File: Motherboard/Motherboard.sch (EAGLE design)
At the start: 12 parts

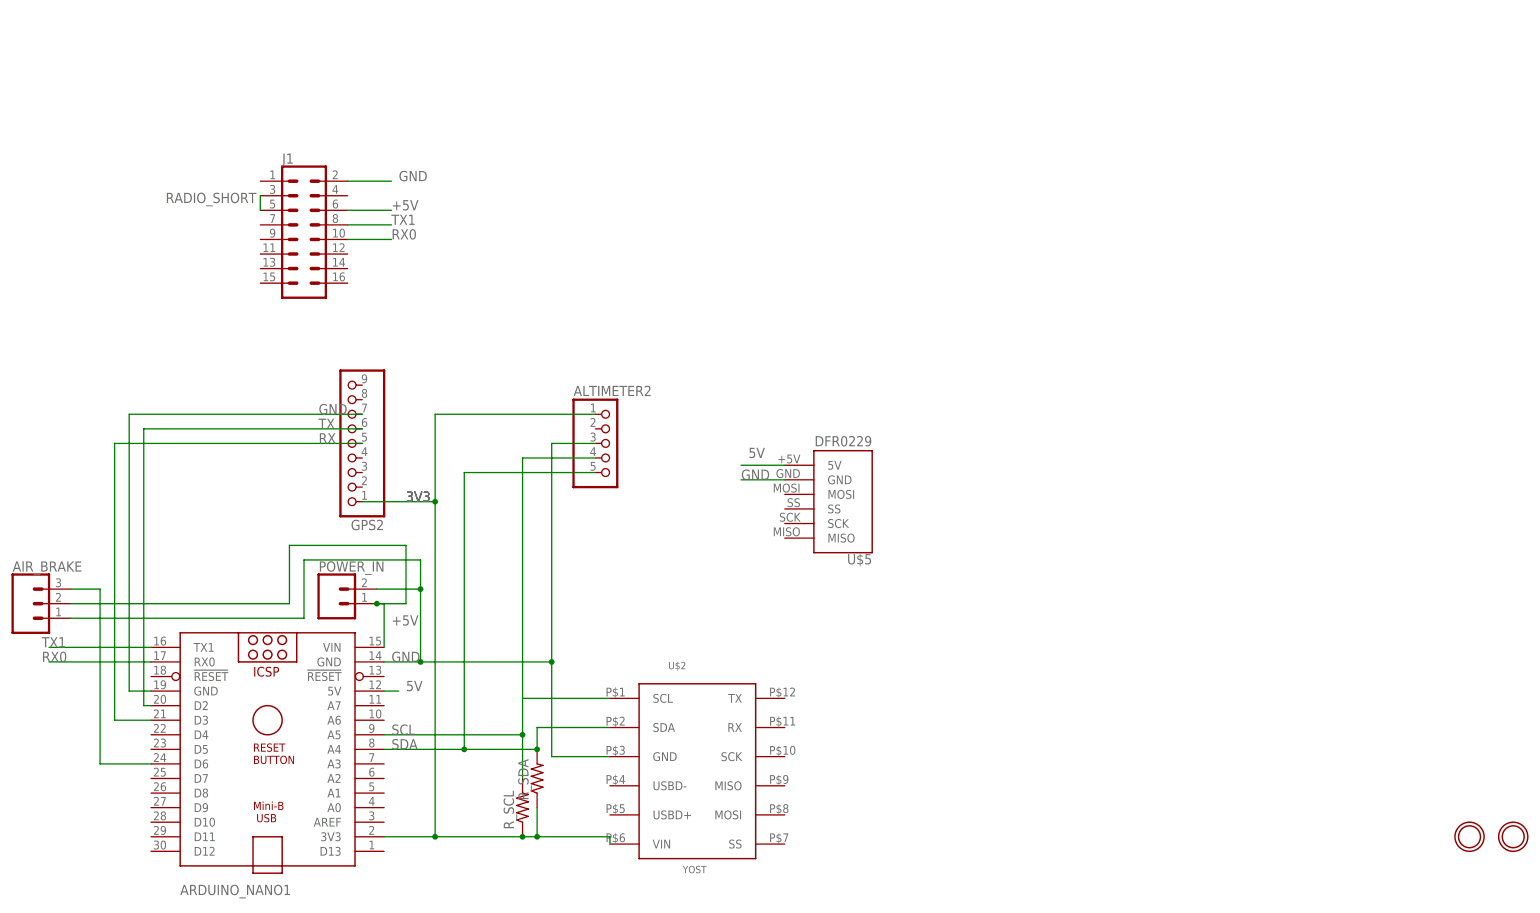
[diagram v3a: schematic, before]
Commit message: add components to boards
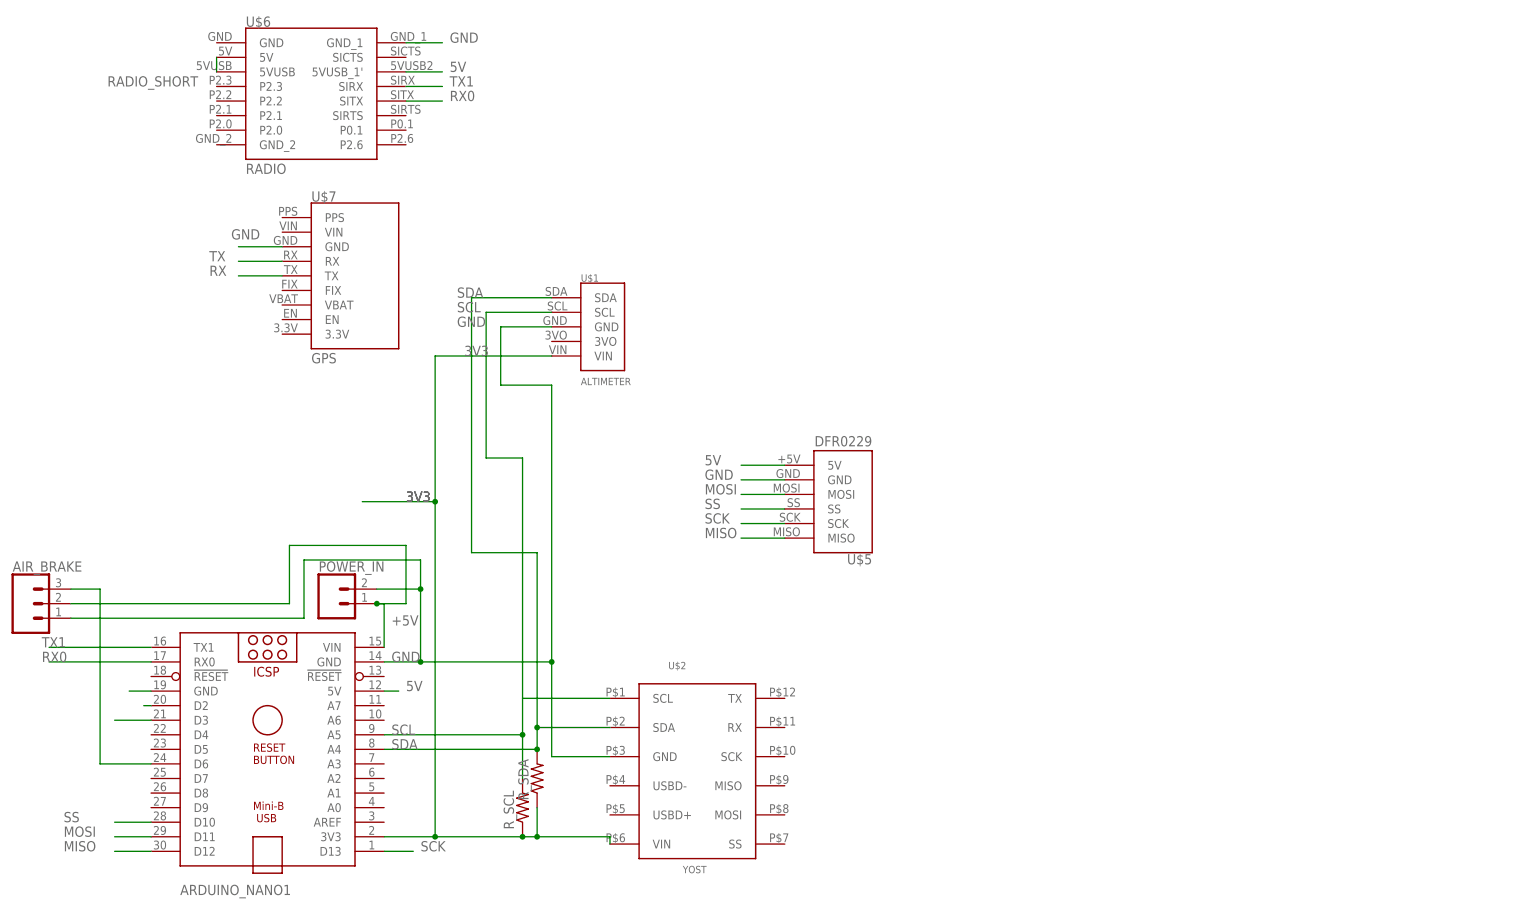
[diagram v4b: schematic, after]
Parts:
- removed ALTIMETER2: (no value), microbuilder:HEADER-1X570MIL
- removed GPS2: (no value), microbuilder:HEADER-1X970MIL
- removed J1: (no value), SparkFun-Connectors:CONN_08X2_HEADER
- removed U$3, U$4: MOUNTINGHOLE2.5, microbuilder:MOUNTINGHOLE2.5
- added U$1: ALTIMETER, uORocketry-parts:ALTIMETER
- added U$6: RADIO, uORocketry-parts:RADIO
- added U$7: GPS, uORocketry-parts:GPS
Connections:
- new net MISO: ARDUINO_NANO1.D12, U$5.MISO
- new net MOSI: ARDUINO_NANO1.D11, U$5.MOSI
- new net SCK: ARDUINO_NANO1.D13, U$5.SCK
- new net SS: ARDUINO_NANO1.D10, U$5.SS
- net +5V: no longer J1.6
- net 3V3: now also U$1.VIN; no longer ALTIMETER2.1, GPS2.1
- net 5V: now also U$6.5VUSB_1'
- net GND: now also U$1.GND, U$6.GND_1, U$7.GND; no longer ALTIMETER2.3, GPS2.7, J1.2
- net RADIO_SHORT: now also U$6.5V, U$6.5VUSB; no longer J1.3, J1.5
- net RX: now also U$7.TX; no longer GPS2.5
- net RX0: now also U$6.SITX; no longer J1.10
- net SCL: now also U$1.SCL; no longer ALTIMETER2.4
- net SDA: now also U$1.SDA; no longer ALTIMETER2.5
- net TX: now also U$7.RX; no longer GPS2.6
- net TX1: now also U$6.SIRX; no longer J1.8

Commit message: more layout
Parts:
- added U$3: RS232, uORocketry-parts:RS232
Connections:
- new net SBG_RX: ARDUINO_NANO1.D5, U$3.RX-1
- new net SBG_TX: ARDUINO_NANO1.D4, U$3.TX-0
- net 5V: now also U$3.VCC
- net GND: now also U$3.GND
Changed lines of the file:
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@@
 <setting verticaltext="up"/>
 </settings>
-<grid distance="0.05" unitdist="inch" unit="inch" style="lines" multiple="1" display="no" altdistance="0.01" altunitdist="inch" altunit="inch"/>
+<grid distance="0.1" unitdist="inch" unit="inch" style="lines" multiple="1" display="no" altdistance="0.01" altunitdist="inch" altunit="inch"/>
 <layers>
 <layer number="1" name="Top" color="4" fill="1" visible="no" active="no"/>
@@
 <part name="U$1" library="uORocketry-parts" deviceset="ALTIMETER" device=""/>
 <part name="U$7" library="uORocketry-parts" deviceset="GPS" device=""/>
+<part name="U$3" library="uORocketry-parts" deviceset="RS232" device=""/>
 </parts>
 <sheets>
@@
 <attribute name="VALUE" x="-34.29" y="57.15" size="1.778" layer="96"/>
 </instance>
+<instance part="U$3" gate="G$1" x="33.02" y="93.98" smashed="yes"/>
 </instances>
 <busses>
@@
 <label x="-48.26" y="78.74" size="1.778" layer="95"/>
 </segment>
+<segment>
+<pinref part="U$3" gate="G$1" pin="GND"/>
+<wire x1="22.86" y1="96.52" x2="15.24" y2="96.52" width="0.1524" layer="91"/>
+<label x="12.7" y="96.52" size="1.778" layer="95"/>
+</segment>
 </net>
 <net name="SDA" class="0">
@@
 <label x="-10.16" y="107.95" size="1.778" layer="95"/>
 </segment>
+<segment>
+<pinref part="U$3" gate="G$1" pin="VCC"/>
+<wire x1="22.86" y1="101.6" x2="15.24" y2="101.6" width="0.1524" layer="91"/>
+<label x="12.7" y="101.6" size="1.778" layer="95"/>
+</segment>
 </net>
 <net name="SCK" class="0">
@@
 </segment>
 </net>
+<net name="SBG_TX" class="0">
+<segment>
+<pinref part="ARDUINO_NANO1" gate="G$1" pin="D4"/>
+<wire x1="-62.23" y1="-7.62" x2="-68.58" y2="-7.62" width="0.1524" layer="91"/>
+<label x="-81.28" y="-7.62" size="1.778" layer="95"/>
+</segment>
+<segment>
+<pinref part="U$3" gate="G$1" pin="TX-0"/>
+<wire x1="22.86" y1="91.44" x2="15.24" y2="91.44" width="0.1524" layer="91"/>
+<label x="5.08" y="91.44" size="1.778" layer="95"/>
+</segment>
+</net>
+<net name="SBG_RX" class="0">
+<segment>
+<pinref part="ARDUINO_NANO1" gate="G$1" pin="D5"/>
+<wire x1="-62.23" y1="-10.16" x2="-68.58" y2="-10.16" width="0.1524" layer="91"/>
+<label x="-81.28" y="-10.16" size="1.778" layer="95"/>
+</segment>
+<segment>
+<pinref part="U$3" gate="G$1" pin="RX-1"/>
+<wire x1="22.86" y1="86.36" x2="15.24" y2="86.36" width="0.1524" layer="91"/>
+<label x="5.08" y="86.36" size="1.778" layer="95"/>
+</segment>
+</net>

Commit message: review1
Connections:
- net SBG_RX: now also ARDUINO_NANO1.D9; no longer ARDUINO_NANO1.D5
- net SBG_TX: now also ARDUINO_NANO1.D8; no longer ARDUINO_NANO1.D4
- net SS: now also ARDUINO_NANO1.D4; no longer ARDUINO_NANO1.D10
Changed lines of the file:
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@@
 <net name="SS" class="0">
-<segment>
-<pinref part="ARDUINO_NANO1" gate="G$1" pin="D10"/>
-<wire x1="-62.23" y1="-22.86" x2="-68.58" y2="-22.86" width="0.1524" layer="91"/>
-<label x="-77.47" y="-22.86" size="1.778" layer="95"/>
-</segment>
 <segment>
 <pinref part="U$5" gate="G$1" pin="SS"/>
@@
 <label x="34.29" y="31.75" size="1.778" layer="95"/>
 </segment>
-</net>
-<net name="SBG_TX" class="0">
 <segment>
 <pinref part="ARDUINO_NANO1" gate="G$1" pin="D4"/>
 <wire x1="-62.23" y1="-7.62" x2="-68.58" y2="-7.62" width="0.1524" layer="91"/>
-<label x="-81.28" y="-7.62" size="1.778" layer="95"/>
+<label x="-76.2" y="-7.62" size="1.778" layer="95"/>
 </segment>
+</net>
+<net name="SBG_TX" class="0">
 <segment>
 <pinref part="U$3" gate="G$1" pin="TX-0"/>
@@
 <label x="5.08" y="91.44" size="1.778" layer="95"/>
 </segment>
+<segment>
+<pinref part="ARDUINO_NANO1" gate="G$1" pin="D8"/>
+<wire x1="-62.23" y1="-17.78" x2="-68.58" y2="-17.78" width="0.1524" layer="91"/>
+<label x="-78.74" y="-17.78" size="1.778" layer="95"/>
+</segment>
 </net>
 <net name="SBG_RX" class="0">
-<segment>
-<pinref part="ARDUINO_NANO1" gate="G$1" pin="D5"/>
-<wire x1="-62.23" y1="-10.16" x2="-68.58" y2="-10.16" width="0.1524" layer="91"/>
-<label x="-81.28" y="-10.16" size="1.778" layer="95"/>
-</segment>
 <segment>
 <pinref part="U$3" gate="G$1" pin="RX-1"/>
@@
 <label x="5.08" y="86.36" size="1.778" layer="95"/>
 </segment>
+<segment>
+<pinref part="ARDUINO_NANO1" gate="G$1" pin="D9"/>
+<wire x1="-62.23" y1="-20.32" x2="-68.58" y2="-20.32" width="0.1524" layer="91"/>
+<label x="-78.74" y="-20.32" size="1.778" layer="95"/>
+</segment>
 </net>
